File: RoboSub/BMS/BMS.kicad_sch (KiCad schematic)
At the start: 30 parts, among them J1 battery, J2 temp, J3 ExtPwrSw, J4 output, J5 CAN, Q1 PMV28ENEA, SW1 DBG2, SW2 DBG1, SW3 RST, U1 VXO7803, U2 CZ3A07, U5 PCC

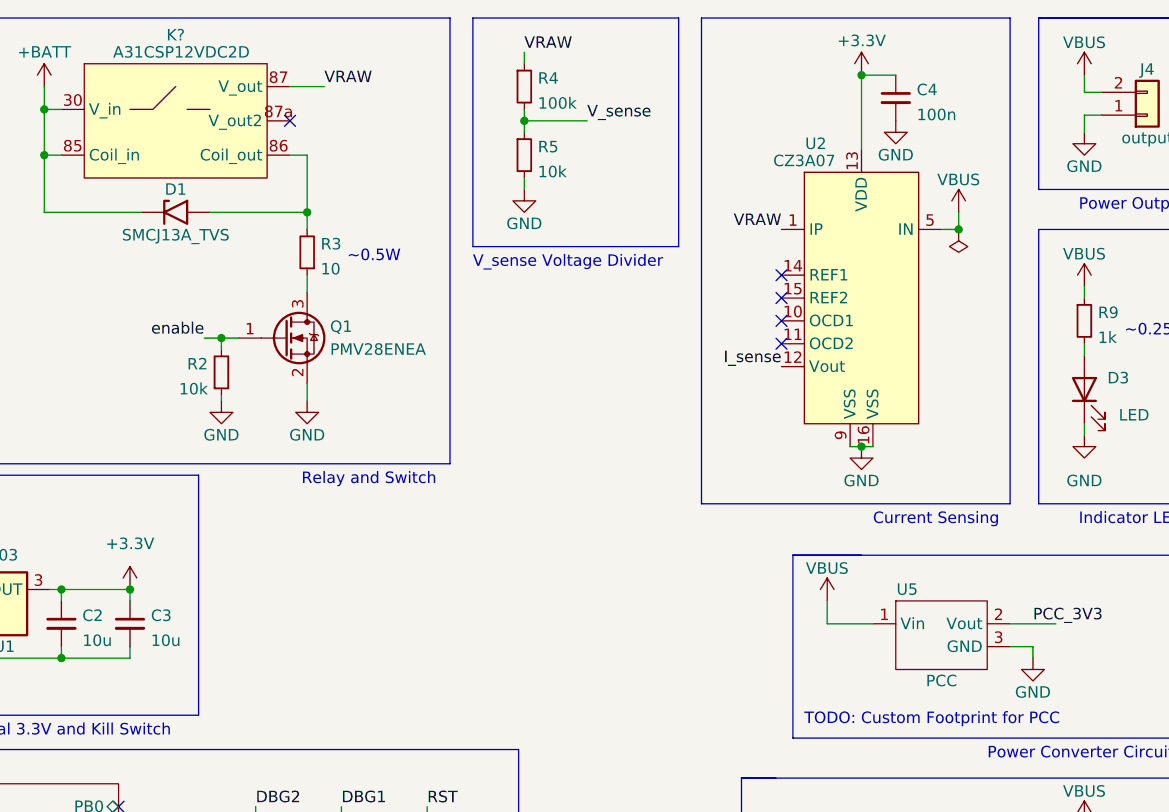
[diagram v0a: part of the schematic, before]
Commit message: PCC added to BMS. TODO: change TVS diode.
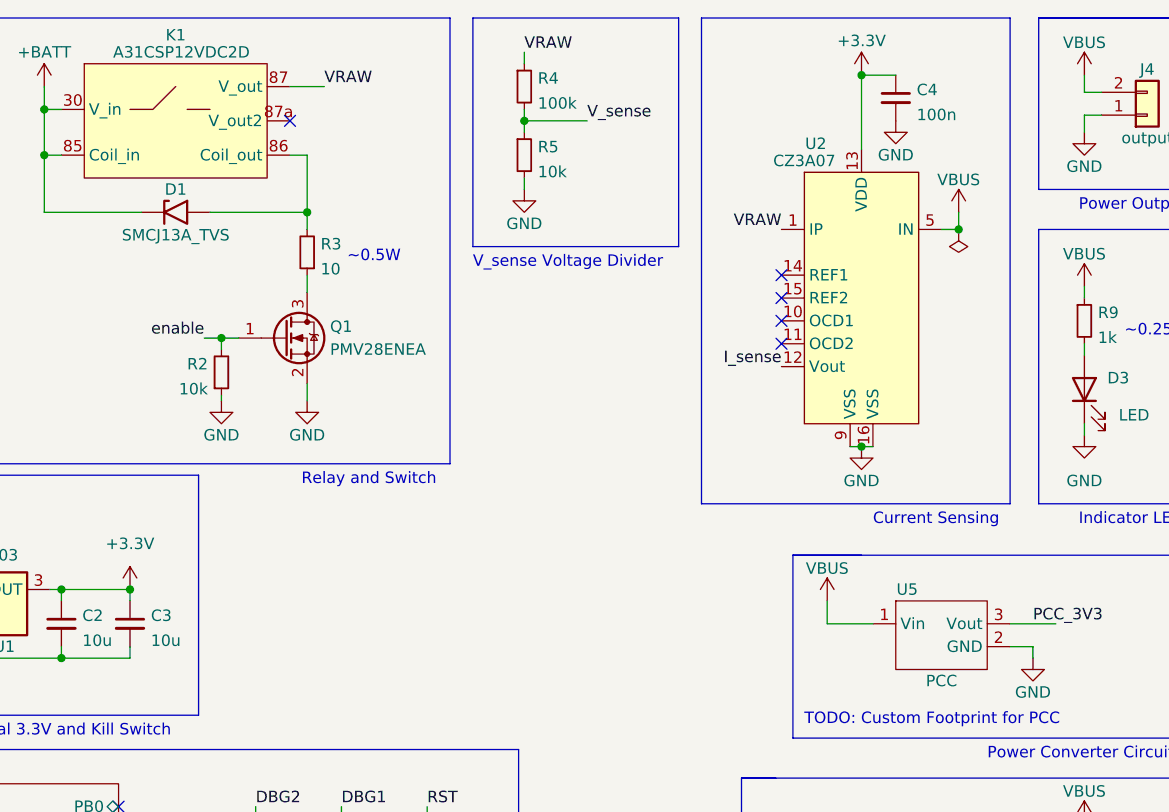
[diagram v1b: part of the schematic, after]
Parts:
- D1: footprint (none) -> Diode_SMD:D_SMC
- U5: footprint (none) -> BMS_Library:PCC_footprint
- gave numbers to parts that had none: 1
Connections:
- net GND: now also U5.2 (GND); no longer U5.3 (GND)
- net PCC_3V3: now also U5.3 (Vout); no longer U5.2 (Vout)
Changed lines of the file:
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@@
   (symbol (lib_id "BMS_Library:A31CSP12VDC2D") (at 113.03 35.56 0) (unit 1)
     (in_bom yes) (on_board yes)
-    (property "Reference" "K?" (id 0) (at 113.03 28.575 0))
+    (property "Reference" "K1" (id 0) (at 113.03 28.575 0))
     (property "Value" "A31CSP12VDC2D" (id 1) (at 113.665 30.48 0))
     (property "Footprint" "BMS_Library:A3_Relay" (id 2) (at 113.03 35.56 0)
@@
     (property "Reference" "U5" (id 0) (at 194.31 90.17 0))
     (property "Value" "PCC" (id 1) (at 198.12 100.33 0))
-    (property "Footprint" "" (id 2) (at 198.12 95.25 0)
+    (property "Footprint" "BMS_Library:PCC_footprint" (id 2) (at 198.12 95.25 0)
       (effects (font (size 1.27 1.27)) hide)
     )
@@
     (property "Reference" "D1" (id 0) (at 113.03 45.72 0))
     (property "Value" "SMCJ13A_TVS" (id 1) (at 113.03 50.8 0))
-    (property "Footprint" "" (id 2) (at 113.03 53.34 0)
+    (property "Footprint" "Diode_SMD:D_SMC" (id 2) (at 113.03 53.34 0)
       (effects (font (size 1.27 1.27)) hide)
     )
@@
     )
     (path "/4a45b954-d385-430f-a2ee-394c29269c8b"
-      (reference "D1") (unit 1) (value "SMCJ13A_TVS") (footprint "")
+      (reference "D1") (unit 1) (value "SMCJ13A_TVS") (footprint "Diode_SMD:D_SMC")
     )
     (path "/00000000-0000-0000-0000-00005e635a64"
@@
     )
     (path "/25ee2213-f0fe-4c7d-ac11-be4f26ffce69"
-      (reference "K?") (unit 1) (value "A31CSP12VDC2D") (footprint "BMS_Library:A3_Relay")
+      (reference "K1") (unit 1) (value "A31CSP12VDC2D") (footprint "BMS_Library:A3_Relay")
     )
     (path "/96040761-b0e5-47a9-8ba7-7d9622476861"
@@
     )
     (path "/3de94952-677f-4939-b835-ffac8620a5f9"
-      (reference "U5") (unit 1) (value "PCC") (footprint "")
-    )
-  )
+      (reference "U5") (unit 1) (value "PCC") (footprint "BMS_Library:PCC_footprint")
+    )
+  )

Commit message: working on layout
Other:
- note removed: "TODO: Custom Footprint for PCC"
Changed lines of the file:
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@@
-    (effects (font (size 1.27 1.27)) (justify left bottom))
-  )
-  (text "TODO: Custom Footprint for PCC" (at 182.88 105.41 0)
     (effects (font (size 1.27 1.27)) (justify left bottom))
   )

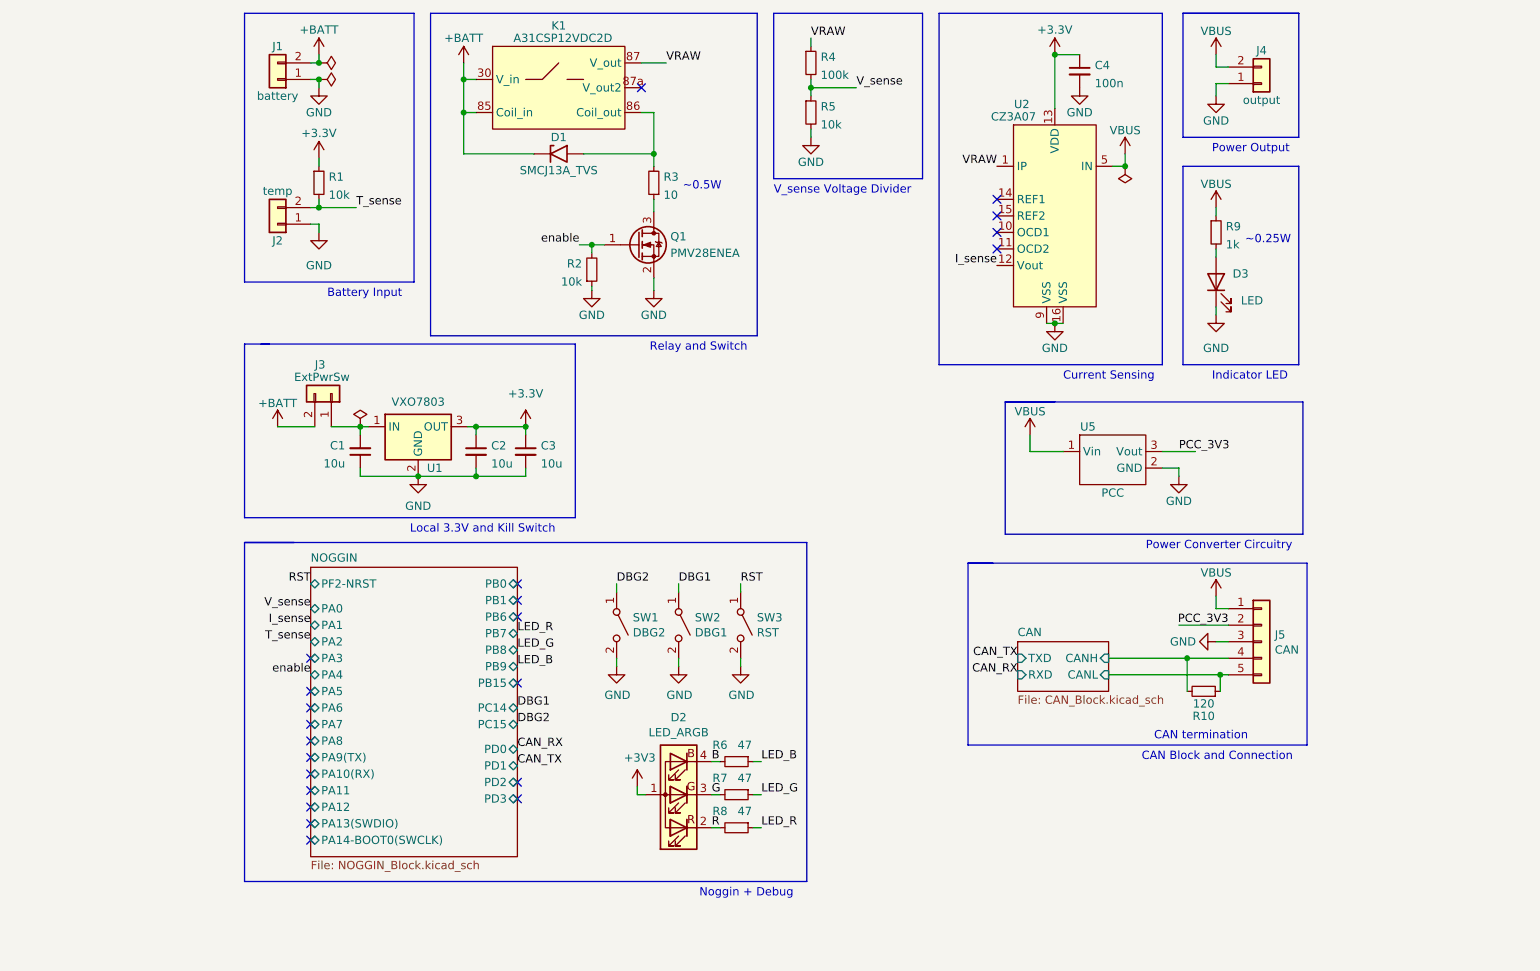
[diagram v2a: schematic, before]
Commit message: updating schematic for 5V current sense
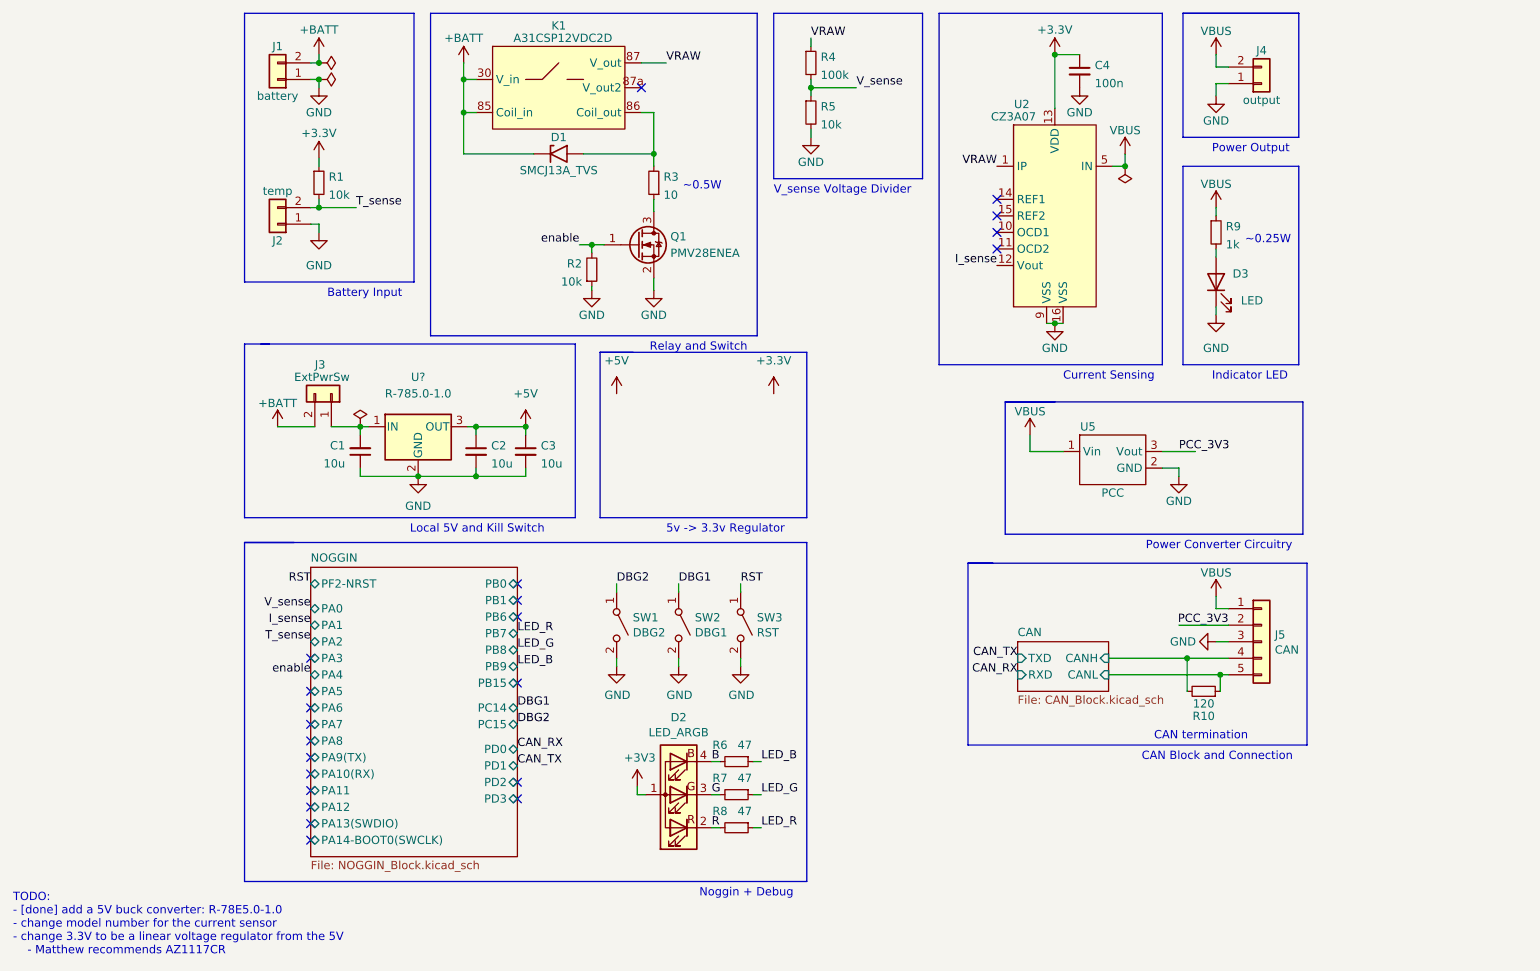
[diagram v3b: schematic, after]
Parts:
- removed U1: VXO7803, Converter_DCDC:Converter_DCDC_Murata_OKI-78SR_Vertical, symbol Converter_DCDC:OKI-78SR-5_1.5-W36-C
- added U?: R-785.0-1.0, Converter_DCDC:Converter_DCDC_RECOM_R-78E-0.5_THT, symbol Regulator_Switching:R-785.0-1.0
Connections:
- net +3V3: no longer C2.1, C3.1
- net GND: now also U?.2 (GND)
- net at C1.2, J3.1 (Pin_1): now also U?.1 (IN)
- new net +5V: C2.1, C3.1, U?.3 (OUT)
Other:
- note added: "5v -> 3.3v Regulator"
- note added: "Local 5V and Kill Switch"
- note added: "TODO: - [done] add a 5V buck converter: R-78E5.0-1.0 - change model number for the current sensor - change 3.3V to be a linear voltage regulator from the 5V - Matthew recommends AZ1117CR"
- note removed: "Local 3.3V and Kill Switch"
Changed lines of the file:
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@@
   (junction (at 76.2 56.515) (diameter 0) (color 0 0 0 0)
   )
+  (junction (at 107.95 90.17) (diameter 0) (color 0 0 0 0)
+  )
   (junction (at 118.11 62.23) (diameter 0) (color 0 0 0 0)
   )
   (junction (at 91.44 97.79) (diameter 0) (color 0 0 0 0)
-  )
-  (junction (at 107.95 90.17) (diameter 0) (color 0 0 0 0)
   )
   (junction (at 127.635 48.26) (diameter 0) (color 0 0 0 0)
@@
     (stroke (width 0) (type default) (color 0 0 0 0))
   )
+  (polyline (pts (xy 119.38 78.74) (xy 124.46 78.74))
+    (stroke (width 0) (type default) (color 0 0 0 0))
+  )
   (wire (pts (xy 82.55 96.52) (xy 82.55 97.79))
     (stroke (width 0) (type default) (color 0 0 0 0))
@@
     (stroke (width 0) (type default) (color 0 0 0 0))
   )
+  (polyline (pts (xy 119.38 78.74) (xy 151.13 78.74))
+    (stroke (width 0) (type default) (color 0 0 0 0))
+  )
   (polyline (pts (xy 226.695 26.67) (xy 226.695 45.72))
     (stroke (width 0) (type default) (color 0 0 0 0))
@@
     (stroke (width 0) (type default) (color 0 0 0 0))
   )
+  (polyline (pts (xy 119.38 104.14) (xy 119.38 78.74))
+    (stroke (width 0) (type default) (color 0 0 0 0))
+  )
+  (polyline (pts (xy 151.13 78.74) (xy 151.13 104.14))
+    (stroke (width 0) (type default) (color 0 0 0 0))
+  )
   (wire (pts (xy 208.28 96.52) (xy 208.28 97.79))
     (stroke (width 0) (type default) (color 0 0 0 0))
@@
     (stroke (width 0) (type default) (color 0 0 0 0))
   )
+  (polyline (pts (xy 151.13 104.14) (xy 119.38 104.14))
+    (stroke (width 0) (type default) (color 0 0 0 0))
+  )
   (wire (pts (xy 214.63 128.27) (xy 214.63 130.81))
     (stroke (width 0) (type default) (color 0 0 0 0))
@@
     (stroke (width 0) (type default) (color 0 0 0 0))
   )
-  (text "Local 3.3V and Kill Switch" (at 90.17 106.68 0)
+  (text "5v -> 3.3v Regulator" (at 129.54 106.68 0)
+    (effects (font (size 1.27 1.27)) (justify left bottom))
+  )
+  (text "Local 5V and Kill Switch" (at 90.17 106.68 0)
     (effects (font (size 1.27 1.27)) (justify left bottom))
   )
@@
   )
   (text "Battery Input" (at 77.47 70.485 0)
+    (effects (font (size 1.27 1.27)) (justify left bottom))
+  )
+  (text "TODO:\n- [done] add a 5V buck converter: R-78E5.0-1.0\n- change model number for the current sensor\n- change 3.3V to be a linear voltage regulator from the 5V\n	- Matthew recommends AZ1117CR\n"
+    (at 29.21 171.45 0)
     (effects (font (size 1.27 1.27)) (justify left bottom))
   )
@@
     (pin "2")
   )
-  (symbol (lib_id "power:+3.3V") (at 107.95 90.17 0) (unit 1)
-    (in_bom yes) (on_board yes) (fields_autoplaced)
-    (property "Reference" "#PWR08" (id 0) (at 107.95 93.98 0)
-      (effects (font (size 1.27 1.27)) hide)
-    )
-    (property "Value" "+3.3V" (id 1) (at 107.95 85.09 0))
-    (property "Footprint" "" (id 2) (at 107.95 90.17 0)
-      (effects (font (size 1.27 1.27)) hide)
-    )
-    (property "Datasheet" "" (id 3) (at 107.95 90.17 0)
+  (symbol (lib_id "power:+3.3V") (at 146.05 85.09 0) (unit 1)
+    (in_bom yes) (on_board yes) (fields_autoplaced)
+    (property "Reference" "#PWR08" (id 0) (at 146.05 88.9 0)
+      (effects (font (size 1.27 1.27)) hide)
+    )
+    (property "Value" "+3.3V" (id 1) (at 146.05 80.01 0))
+    (property "Footprint" "" (id 2) (at 146.05 85.09 0)
+      (effects (font (size 1.27 1.27)) hide)
+    )
+    (property "Datasheet" "" (id 3) (at 146.05 85.09 0)
       (effects (font (size 1.27 1.27)) hide)
     )
@@
     (pin "2")
   )
+  (symbol (lib_id "Regulator_Switching:R-785.0-1.0") (at 91.44 90.17 0) (unit 1)
+    (in_bom yes) (on_board yes) (fields_autoplaced)
+    (property "Reference" "U?" (id 0) (at 91.44 82.55 0))
+    (property "Value" "R-785.0-1.0" (id 1) (at 91.44 85.09 0))
+    (property "Footprint" "Converter_DCDC:Converter_DCDC_RECOM_R-78E-0.5_THT" (id 2) (at 92.71 96.52 0)
+      (effects (font (size 1.27 1.27) italic) (justify left) hide)
+    )
+    (property "Datasheet" "https://www.recom-power.com/pdf/Innoline/R-78xx-1.0.pdf" (id 3) (at 91.44 90.17 0)
+      (effects (font (size 1.27 1.27)) hide)
+    )
+    (pin "1")
+    (pin "2")
+    (pin "3")
+  )
   (symbol (lib_id "BMS_Library:PCC") (at 198.12 95.25 0) (unit 1)
     (in_bom yes) (on_board yes)
@@
     (pin "2")
     (pin "3")
+  )
+  (symbol (lib_id "power:+5V") (at 107.95 90.17 0) (unit 1)
+    (in_bom yes) (on_board yes) (fields_autoplaced)
+    (property "Reference" "#PWR?" (id 0) (at 107.95 93.98 0)
+      (effects (font (size 1.27 1.27)) hide)
+    )
+    (property "Value" "+5V" (id 1) (at 107.95 85.09 0))
+    (property "Footprint" "" (id 2) (at 107.95 90.17 0)
+      (effects (font (size 1.27 1.27)) hide)
+    )
+    (property "Datasheet" "" (id 3) (at 107.95 90.17 0)
+      (effects (font (size 1.27 1.27)) hide)
+    )
+    (pin "1")
   )
   (symbol (lib_id "Device:R_Small") (at 118.11 66.04 0) (mirror x) (unit 1)
@@
     (pin "1")
   )
-  (symbol (lib_id "Converter_DCDC:OKI-78SR-5_1.5-W36-C") (at 91.44 90.17 0) (unit 1)
-    (in_bom yes) (on_board yes)
-    (property "Reference" "U1" (id 0) (at 93.98 96.52 0))
-    (property "Value" "VXO7803" (id 1) (at 91.44 86.36 0))
-    (property "Footprint" "Converter_DCDC:Converter_DCDC_Murata_OKI-78SR_Vertical" (id 2) (at 92.71 96.52 0)
-      (effects (font (size 1.27 1.27) italic) (justify left) hide)
-    )
-    (property "Datasheet" "https://power.murata.com/data/power/oki-78sr.pdf" (id 3) (at 91.44 90.17 0)
-      (effects (font (size 1.27 1.27)) hide)
-    )
-    (pin "1")
-    (pin "2")
-    (pin "3")
-  )
   (symbol (lib_id "power:GND") (at 76.2 60.325 0) (unit 1)
     (in_bom yes) (on_board yes) (fields_autoplaced)
@@
     (pin "1")
     (pin "2")
+  )
+  (symbol (lib_id "power:+5V") (at 121.92 85.09 0) (unit 1)
+    (in_bom yes) (on_board yes) (fields_autoplaced)
+    (property "Reference" "#PWR?" (id 0) (at 121.92 88.9 0)
+      (effects (font (size 1.27 1.27)) hide)
+    )
+    (property "Value" "+5V" (id 1) (at 121.92 80.01 0))
+    (property "Footprint" "" (id 2) (at 121.92 85.09 0)
+      (effects (font (size 1.27 1.27)) hide)
+    )
+    (property "Datasheet" "" (id 3) (at 121.92 85.09 0)
+      (effects (font (size 1.27 1.27)) hide)
+    )
+    (pin "1")
   )
   (symbol (lib_id "power:GND") (at 193.04 38.1 0) (unit 1)
@@
       (reference "#PWR0102") (unit 1) (value "VBUS") (footprint "")
     )
+    (path "/3f5c93cf-78d4-4f9e-8350-f85d6ccb7e44"
+      (reference "#PWR?") (unit 1) (value "+5V") (footprint "")
+    )
+    (path "/e9e3ce6c-17f7-4fee-b4ca-218fac63a4dd"
+      (reference "#PWR?") (unit 1) (value "+5V") (footprint "")
+    )
     (path "/12b82ebf-c6d2-4bb6-a68b-404835dbf140"
       (reference "C1") (unit 1) (value "10u") (footprint "Capacitor_SMD:C_0805_2012Metric")
@@
       (reference "SW3") (unit 1) (value "RST") (footprint "Button_Switch_SMD:SW_SPST_PTS810")
     )
-    (path "/b39daa9e-c35d-43d8-815a-05d9d1790cb1"
-      (reference "U1") (unit 1) (value "VXO7803") (footprint "Converter_DCDC:Converter_DCDC_Murata_OKI-78SR_Vertical")
-    )
     (path "/734800e8-1d75-489d-a5c7-acc392b686a9"
       (reference "U2") (unit 1) (value "CZ3A07") (footprint "BMS_Library:CZ3AG7_HalEfSens")
@@
       (reference "U5") (unit 1) (value "PCC") (footprint "BMS_Library:PCC_footprint")
     )
-  )
+    (path "/3b467ccd-b746-48a4-9a74-62ccadd74bc5"
+      (reference "U?") (unit 1) (value "R-785.0-1.0") (footprint "Converter_DCDC:Converter_DCDC_RECOM_R-78E-0.5_THT")
+    )
+  )
